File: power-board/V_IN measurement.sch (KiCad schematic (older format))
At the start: 9 parts, among them U2 TLV521

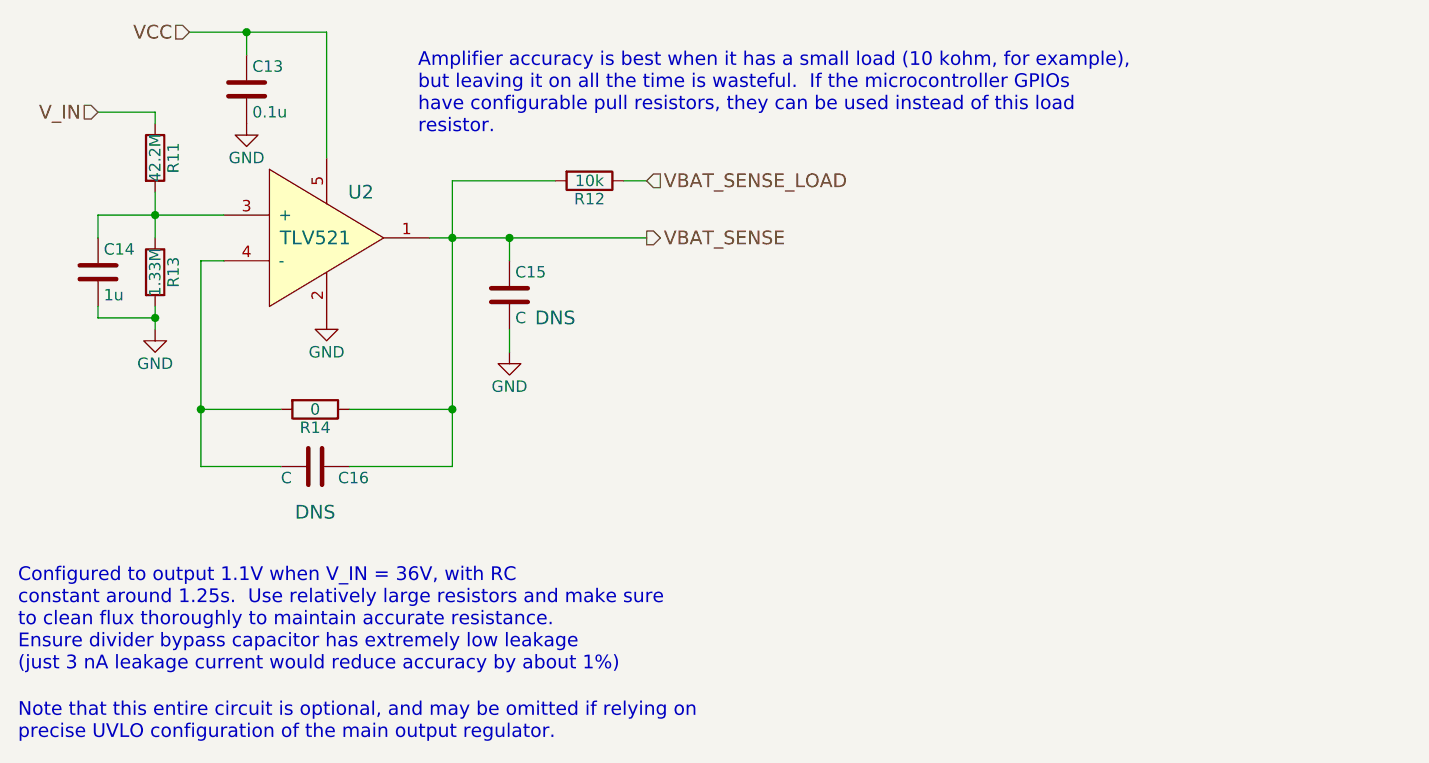
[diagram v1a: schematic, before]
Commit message: switched to XMEGA A4U
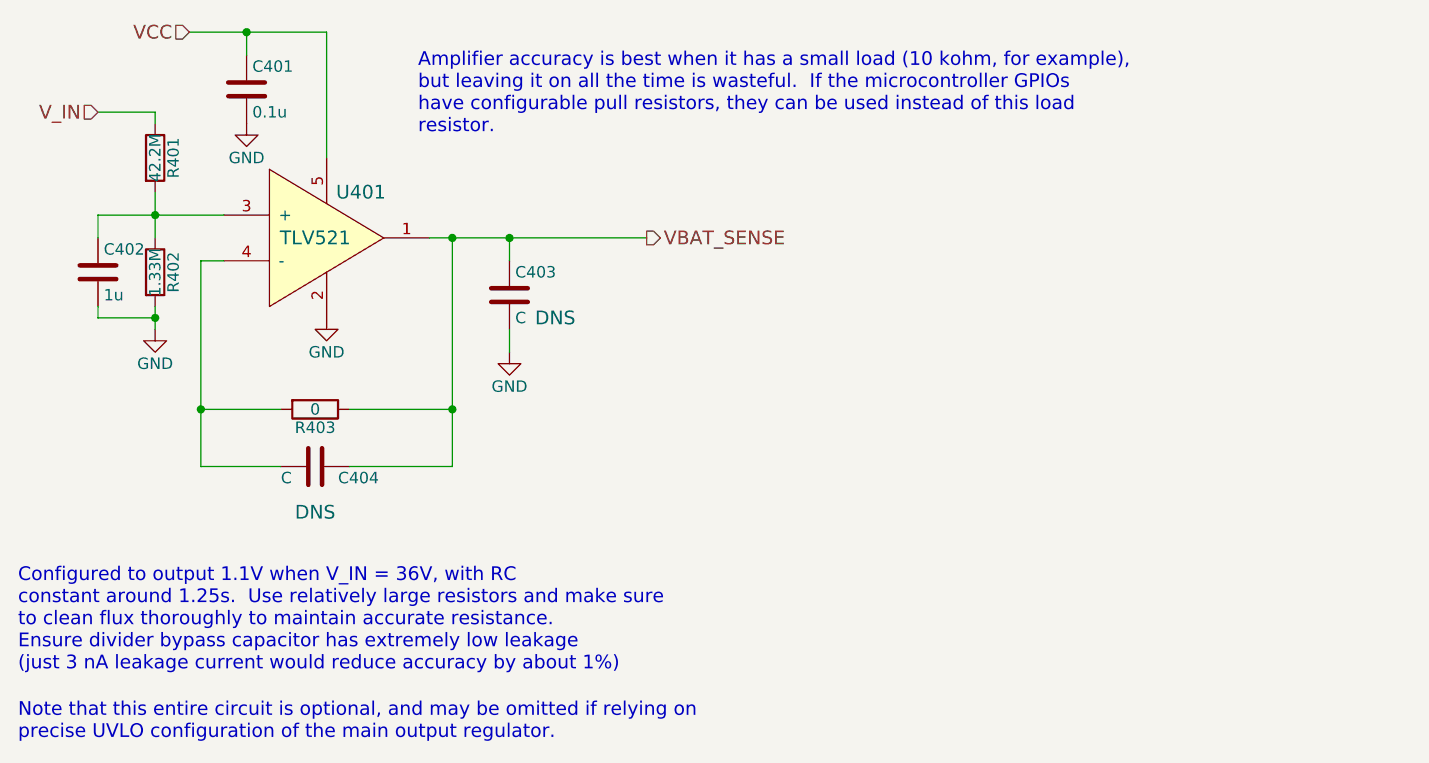
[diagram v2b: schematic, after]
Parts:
- removed R12: 10k, symbol R
- renumbered C13 to C401, C14 to C402, C15 to C403, C16 to C404, R11 to R401, R13 to R402, R14 to R403, U2 to U401
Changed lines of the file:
@@
 $Descr A4 11693 8268
 encoding utf-8
-Sheet 4 10
+Sheet 4 11
 Title ""
 Date ""
@@
 $EndDescr
 $Comp
-L TLV521 U2
+L TLV521 U401
 U 1 1 59352BB4
 P 5200 2800
-F 0 "U2" H 5350 3000 60  0000 C CNN
+F 0 "U401" H 5350 3000 60  0000 C CNN
 F 1 "TLV521" H 5150 2800 60  0000 C CNN
 F 2 "" H 5650 2300 60  0000 C CNN
@@
 $EndComp
 $Comp
-L R R11
+L R R401
 U 1 1 59352C09
 P 4450 2450
-F 0 "R11" V 4530 2450 50  0000 C CNN
+F 0 "R401" V 4530 2450 50  0000 C CNN
 F 1 "42.2M" V 4450 2450 50  0000 C CNN
 F 2 "" V 4380 2450 50  0000 C CNN
@@
 $EndComp
 $Comp
-L R R13
+L R R402
 U 1 1 59352C74
 P 4450 2950
-F 0 "R13" V 4530 2950 50  0000 C CNN
+F 0 "R402" V 4530 2950 50  0000 C CNN
 F 1 "1.33M" V 4450 2950 50  0000 C CNN
 F 2 "" V 4380 2950 50  0000 C CNN
@@
 $EndComp
 $Comp
-L R R14
+L R R403
 U 1 1 59352C9D
 P 5150 3550
-F 0 "R14" V 5230 3550 50  0000 C CNN
+F 0 "R403" V 5230 3550 50  0000 C CNN
 F 1 "0" V 5150 3550 50  0000 C CNN
 F 2 "" V 5080 3550 50  0000 C CNN
@@
 $EndComp
 $Comp
-L C C16
+L C C404
 U 1 1 59352CE0
 P 5150 3800
-F 0 "C16" V 5200 3900 50  0000 L CNN
+F 0 "C404" V 5200 3900 50  0000 L CNN
 F 1 "C" V 5200 3650 50  0000 L CNN
 F 2 "" H 5188 3650 50  0000 C CNN
@@
 $EndComp
 $Comp
-L C C14
+L C C402
 U 1 1 59352D63
 P 4200 2950
-F 0 "C14" H 4225 3050 50  0000 L CNN
+F 0 "C402" H 4225 3050 50  0000 L CNN
 F 1 "1u" H 4225 2850 50  0000 L CNN
 F 2 "" H 4238 2800 50  0000 C CNN
@@
 $EndComp
 $Comp
-L GND #PWR20
+L GND #PWR022
 U 1 1 59352E84
 P 5200 3150
-F 0 "#PWR20" H 5200 2900 50  0001 C CNN
+F 0 "#PWR022" H 5200 2900 50  0001 C CNN
 F 1 "GND" H 5200 3000 50  0000 C CNN
 F 2 "" H 5200 3150 50  0000 C CNN
@@
 VCC
 $Comp
-L C C13
+L C C401
 U 1 1 59352EDA
 P 4850 2150
-F 0 "C13" H 4875 2250 50  0000 L CNN
+F 0 "C401" H 4875 2250 50  0000 L CNN
 F 1 "0.1u" H 4875 2050 50  0000 L CNN
 F 2 "" H 4888 2000 50  0000 C CNN
@@
 $EndComp
 $Comp
-L C C15
+L C C403
 U 1 1 59352F5C
 P 6000 3050
-F 0 "C15" H 6025 3150 50  0000 L CNN
+F 0 "C403" H 6025 3150 50  0000 L CNN
 F 1 "C" H 6025 2950 50  0000 L CNN
 F 2 "" H 6038 2900 50  0000 C CNN
@@
 	5750 3800 5300 3800
 Wire Wire Line
-	5750 2550 5750 3800
-Wire Wire Line
 	5650 2800 6600 2800
 Wire Wire Line
@@
 	6000 3300 6000 3200
 $Comp
-L GND #PWR22
+L GND #PWR023
 U 1 1 593532D3
 P 6000 3300
-F 0 "#PWR22" H 6000 3050 50  0001 C CNN
+F 0 "#PWR023" H 6000 3050 50  0001 C CNN
 F 1 "GND" H 6000 3150 50  0000 C CNN
 F 2 "" H 6000 3300 50  0000 C CNN
@@
 $EndComp
 $Comp
-L GND #PWR21
+L GND #PWR024
 U 1 1 593532F6
 P 4450 3200
-F 0 "#PWR21" H 4450 2950 50  0001 C CNN
+F 0 "#PWR024" H 4450 2950 50  0001 C CNN
 F 1 "GND" H 4450 3050 50  0000 C CNN
 F 2 "" H 4450 3200 50  0000 C CNN
@@
 Configured to output 1.1V when V_IN = 36V, with RC\nconstant around 1.25s.  Use relatively large resistors and make sure\nto clean flux thoroughly to maintain accurate resistance.\nEnsure divider bypass capacitor has extremely low leakage\n(just 3 nA leakage current would reduce accuracy by about 1%)
 $Comp
-L GND #PWR19
+L GND #PWR025
 U 1 1 59353695
 P 4850 2300
-F 0 "#PWR19" H 4850 2050 50  0001 C CNN
+F 0 "#PWR025" H 4850 2050 50  0001 C CNN
 F 1 "GND" H 4850 2150 50  0000 C CNN
 F 2 "" H 4850 2300 50  0000 C CNN
@@
 VBAT_SENSE
 Connection ~ 6000 2800
-$Comp
-L R R12
-U 1 1 59353DEC
-P 6350 2550
-F 0 "R12" V 6430 2550 50  0000 C CNN
-F 1 "10k" V 6350 2550 50  0000 C CNN
-F 2 "" V 6280 2550 50  0000 C CNN
-F 3 "" H 6350 2550 50  0000 C CNN
-F 4 "Vishay" V 6350 2550 60  0001 C CNN "MFG"
-F 5 "CRCW060310K0FKEA" V 6350 2550 60  0001 C CNN "MPN"
-	1    6350 2550
-	0    1    1    0
-$EndComp
-Text HLabel 6600 2550 2    60   Input ~ 0
-VBAT_SENSE_LOAD
-Wire Wire Line
-	6600 2550 6500 2550
-Wire Wire Line
-	6200 2550 5750 2550
 Text Notes 5600 2350 0    60   ~ 0
 Amplifier accuracy is best when it has a small load (10 kohm, for example),\nbut leaving it on all the time is wasteful.  If the microcontroller GPIOs\nhave configurable pull resistors, they can be used instead of this load\nresistor.
 Text Notes 3850 5000 0    60   ~ 0
 Note that this entire circuit is optional, and may be omitted if relying on\nprecise UVLO configuration of the main output regulator.
+Wire Wire Line
+	5750 2800 5750 3800
 $EndSCHEMATC

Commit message: routed board
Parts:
- C401, C402, C403, C404: footprint (none) -> Capacitors_SMD:C_0603
- R401: value 42.2M -> 10M; footprint (none) -> Resistors_SMD:R_0805; MFG (none) -> Yageo; MPN (none) -> RC0805FR-0710ML; Note (none) -> 1%
- R402: value 1.33M -> 316k; footprint (none) -> Resistors_SMD:R_0805; MFG Vishay -> Yageo; MPN CRCW06031M33FKEA -> RC0805FR-07316KL; Note (none) -> 1%
- R403: footprint (none) -> Resistors_SMD:R_0603
- U401: footprint (none) -> TO_SOT_Packages_SMD:SOT-353_SC-70-5
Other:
- moved on the sheet: C402
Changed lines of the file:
@@
 $Descr A4 11693 8268
 encoding utf-8
-Sheet 4 11
+Sheet 4 12
 Title ""
 Date ""
@@
 F 0 "U401" H 5350 3000 60  0000 C CNN
 F 1 "TLV521" H 5150 2800 60  0000 C CNN
-F 2 "" H 5650 2300 60  0000 C CNN
+F 2 "TO_SOT_Packages_SMD:SOT-353_SC-70-5" H 5650 2300 60  0001 C CNN
 F 3 "" H 5650 2300 60  0000 C CNN
 F 4 "Texas Instruments" H 5200 2800 60  0001 C CNN "MFG"
@@
 P 4450 2450
 F 0 "R401" V 4530 2450 50  0000 C CNN
-F 1 "42.2M" V 4450 2450 50  0000 C CNN
-F 2 "" V 4380 2450 50  0000 C CNN
+F 1 "10M" V 4450 2450 50  0000 C CNN
+F 2 "Resistors_SMD:R_0805" V 4380 2450 50  0001 C CNN
 F 3 "" H 4450 2450 50  0000 C CNN
+F 4 "1%" V 4350 2450 60  0000 C CNN "Note"
+F 5 "Yageo" V 4450 2450 60  0001 C CNN "MFG"
+F 6 "RC0805FR-0710ML" V 4450 2450 60  0001 C CNN "MPN"
 	1    4450 2450
 	1    0    0    -1
@@
 P 4450 2950
 F 0 "R402" V 4530 2950 50  0000 C CNN
-F 1 "1.33M" V 4450 2950 50  0000 C CNN
-F 2 "" V 4380 2950 50  0000 C CNN
+F 1 "316k" V 4450 2950 50  0000 C CNN
+F 2 "Resistors_SMD:R_0805" V 4380 2950 50  0001 C CNN
 F 3 "" H 4450 2950 50  0000 C CNN
-F 4 "Vishay" V 4450 2950 60  0001 C CNN "MFG"
-F 5 "CRCW06031M33FKEA" V 4450 2950 60  0001 C CNN "MPN"
+F 4 "Yageo" V 4450 2950 60  0001 C CNN "MFG"
+F 5 "RC0805FR-07316KL" V 4450 2950 60  0001 C CNN "MPN"
+F 6 "1%" V 4350 2950 60  0000 C CNN "Note"
 	1    4450 2950
 	1    0    0    -1
@@
 F 0 "R403" V 5230 3550 50  0000 C CNN
 F 1 "0" V 5150 3550 50  0000 C CNN
-F 2 "" V 5080 3550 50  0000 C CNN
+F 2 "Resistors_SMD:R_0603" V 5080 3550 50  0001 C CNN
 F 3 "" H 5150 3550 50  0000 C CNN
 	1    5150 3550
@@
 F 0 "C404" V 5200 3900 50  0000 L CNN
 F 1 "C" V 5200 3650 50  0000 L CNN
-F 2 "" H 5188 3650 50  0000 C CNN
+F 2 "Capacitors_SMD:C_0603" H 5188 3650 50  0001 C CNN
 F 3 "" H 5150 3800 50  0000 C CNN
 F 4 "DNS" V 5350 3800 60  0000 C CNN "Note"
@@
 L C C402
 U 1 1 59352D63
-P 4200 2950
-F 0 "C402" H 4225 3050 50  0000 L CNN
-F 1 "1u" H 4225 2850 50  0000 L CNN
-F 2 "" H 4238 2800 50  0000 C CNN
-F 3 "" H 4200 2950 50  0000 C CNN
-F 4 "Samsung" H 4200 2950 60  0001 C CNN "MFG"
-F 5 "CL10B105KO8NNNC" H 4200 2950 60  0001 C CNN "MPN"
-	1    4200 2950
+P 4000 2950
+F 0 "C402" H 4025 3050 50  0000 L CNN
+F 1 "1u" H 4025 2850 50  0000 L CNN
+F 2 "Capacitors_SMD:C_0603" H 4038 2800 50  0001 C CNN
+F 3 "" H 4000 2950 50  0000 C CNN
+F 4 "Samsung" H 4000 2950 60  0001 C CNN "MFG"
+F 5 "CL10B105KO8NNNC" H 4000 2950 60  0001 C CNN "MPN"
+	1    4000 2950
 	1    0    0    -1
 $EndComp
 $Comp
-L GND #PWR022
+L GND #PWR09
 U 1 1 59352E84
 P 5200 3150
-F 0 "#PWR022" H 5200 2900 50  0001 C CNN
+F 0 "#PWR09" H 5200 2900 50  0001 C CNN
 F 1 "GND" H 5200 3000 50  0000 C CNN
 F 2 "" H 5200 3150 50  0000 C CNN
@@
 F 0 "C401" H 4875 2250 50  0000 L CNN
 F 1 "0.1u" H 4875 2050 50  0000 L CNN
-F 2 "" H 4888 2000 50  0000 C CNN
+F 2 "Capacitors_SMD:C_0603" H 4888 2000 50  0001 C CNN
 F 3 "" H 4850 2150 50  0000 C CNN
 F 4 "Murata Electronics" H 4850 2150 60  0001 C CNN "MFG"
@@
 F 0 "C403" H 6025 3150 50  0000 L CNN
 F 1 "C" H 6025 2950 50  0000 L CNN
-F 2 "" H 6038 2900 50  0000 C CNN
+F 2 "Capacitors_SMD:C_0603" H 6038 2900 50  0001 C CNN
 F 3 "" H 6000 3050 50  0000 C CNN
 F 4 "DNS" H 6200 2950 60  0000 C CNN "Note"
@@
 	6000 3300 6000 3200
 $Comp
-L GND #PWR023
+L GND #PWR010
 U 1 1 593532D3
 P 6000 3300
-F 0 "#PWR023" H 6000 3050 50  0001 C CNN
+F 0 "#PWR010" H 6000 3050 50  0001 C CNN
 F 1 "GND" H 6000 3150 50  0000 C CNN
 F 2 "" H 6000 3300 50  0000 C CNN
@@
 $EndComp
 $Comp
-L GND #PWR024
+L GND #PWR011
 U 1 1 593532F6
 P 4450 3200
-F 0 "#PWR024" H 4450 2950 50  0001 C CNN
+F 0 "#PWR011" H 4450 2950 50  0001 C CNN
 F 1 "GND" H 4450 3050 50  0000 C CNN
 F 2 "" H 4450 3200 50  0000 C CNN
@@
 	4450 3100 4450 3200
 Wire Wire Line
-	4450 3150 4200 3150
+	4450 3150 4000 3150
 Wire Wire Line
-	4200 3150 4200 3100
+	4000 3150 4000 3100
 Connection ~ 4450 3150
 Wire Wire Line
 	4450 2600 4450 2800
 Wire Wire Line
-	4200 2700 4750 2700
+	4000 2700 4750 2700
 Connection ~ 4450 2700
 Wire Wire Line
-	4200 2700 4200 2800
+	4000 2700 4000 2800
 Wire Wire Line
 	4450 2300 4450 2250
@@
 Configured to output 1.1V when V_IN = 36V, with RC\nconstant around 1.25s.  Use relatively large resistors and make sure\nto clean flux thoroughly to maintain accurate resistance.\nEnsure divider bypass capacitor has extremely low leakage\n(just 3 nA leakage current would reduce accuracy by about 1%)
 $Comp
-L GND #PWR025
+L GND #PWR012
 U 1 1 59353695
 P 4850 2300
-F 0 "#PWR025" H 4850 2050 50  0001 C CNN
+F 0 "#PWR012" H 4850 2050 50  0001 C CNN
 F 1 "GND" H 4850 2150 50  0000 C CNN
 F 2 "" H 4850 2300 50  0000 C CNN

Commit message: adding more part numbers
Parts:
- R403: MFG (none) -> Yageo; MPN (none) -> RC0603JR-070RL
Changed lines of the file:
@@
 $Descr A4 11693 8268
 encoding utf-8
-Sheet 4 12
+Sheet 3 12
 Title ""
 Date ""
@@
 F 2 "Resistors_SMD:R_0603" V 5080 3550 50  0001 C CNN
 F 3 "" H 5150 3550 50  0000 C CNN
+F 4 "Yageo" V 5150 3550 60  0001 C CNN "MFG"
+F 5 "RC0603JR-070RL" V 5150 3550 60  0001 C CNN "MPN"
 	1    5150 3550
 	0    1    1    0
